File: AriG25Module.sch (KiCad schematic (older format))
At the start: 9 parts

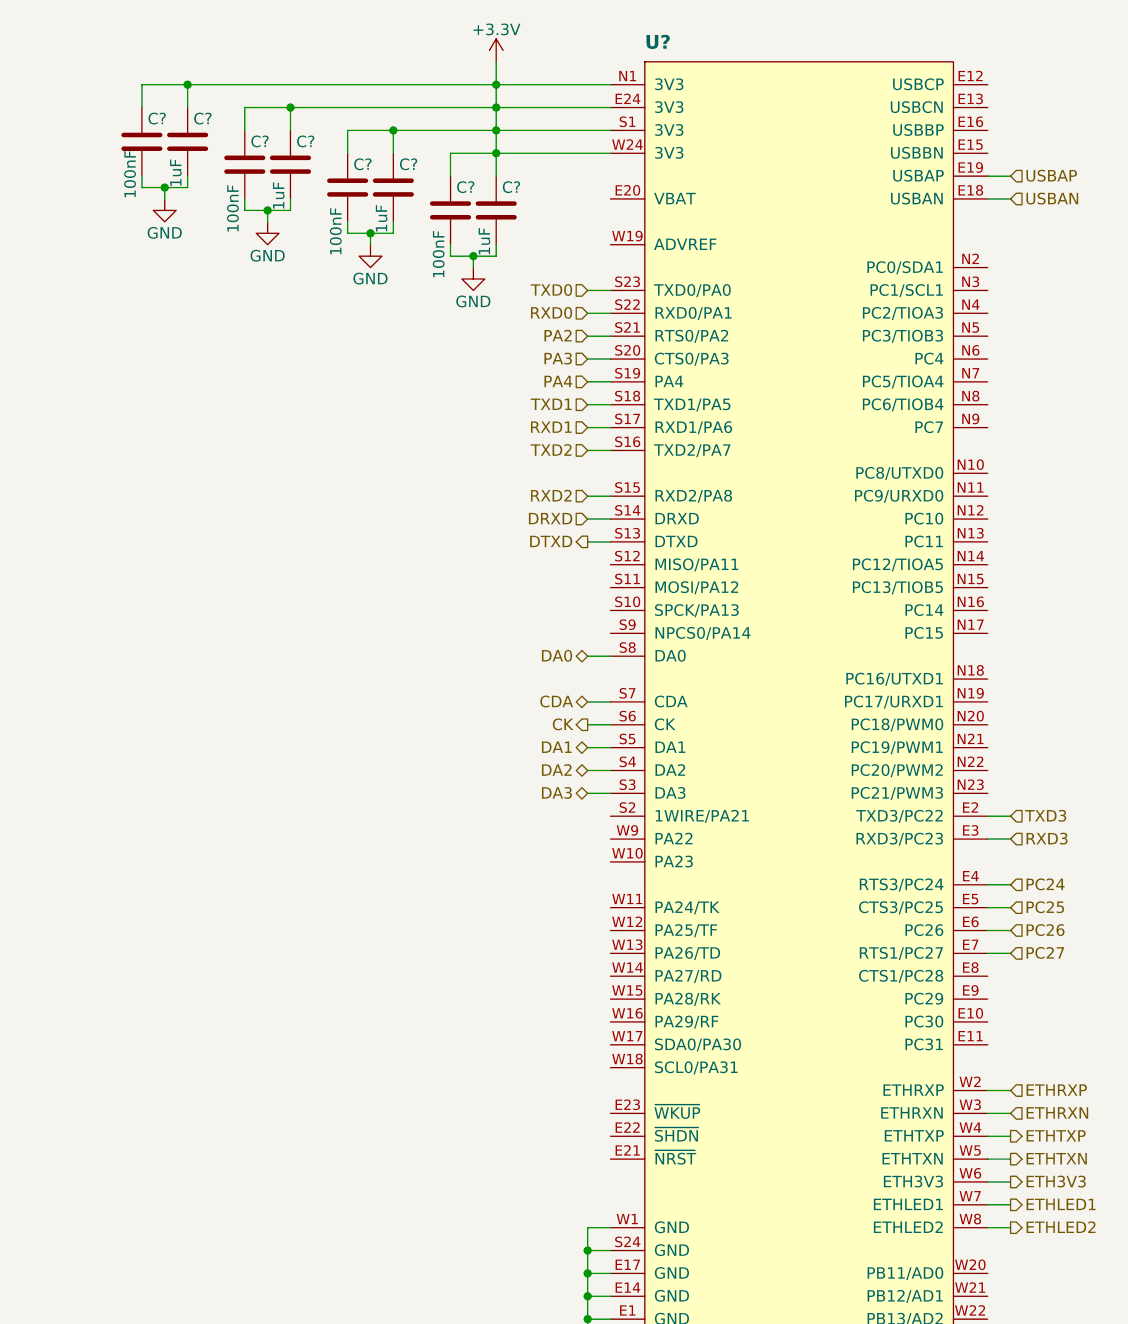
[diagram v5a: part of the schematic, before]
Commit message: Added to scheamtic.
Added reset circuit for Aiya, power led for 3V3 line, USB type A connectors for USBB and USBC.
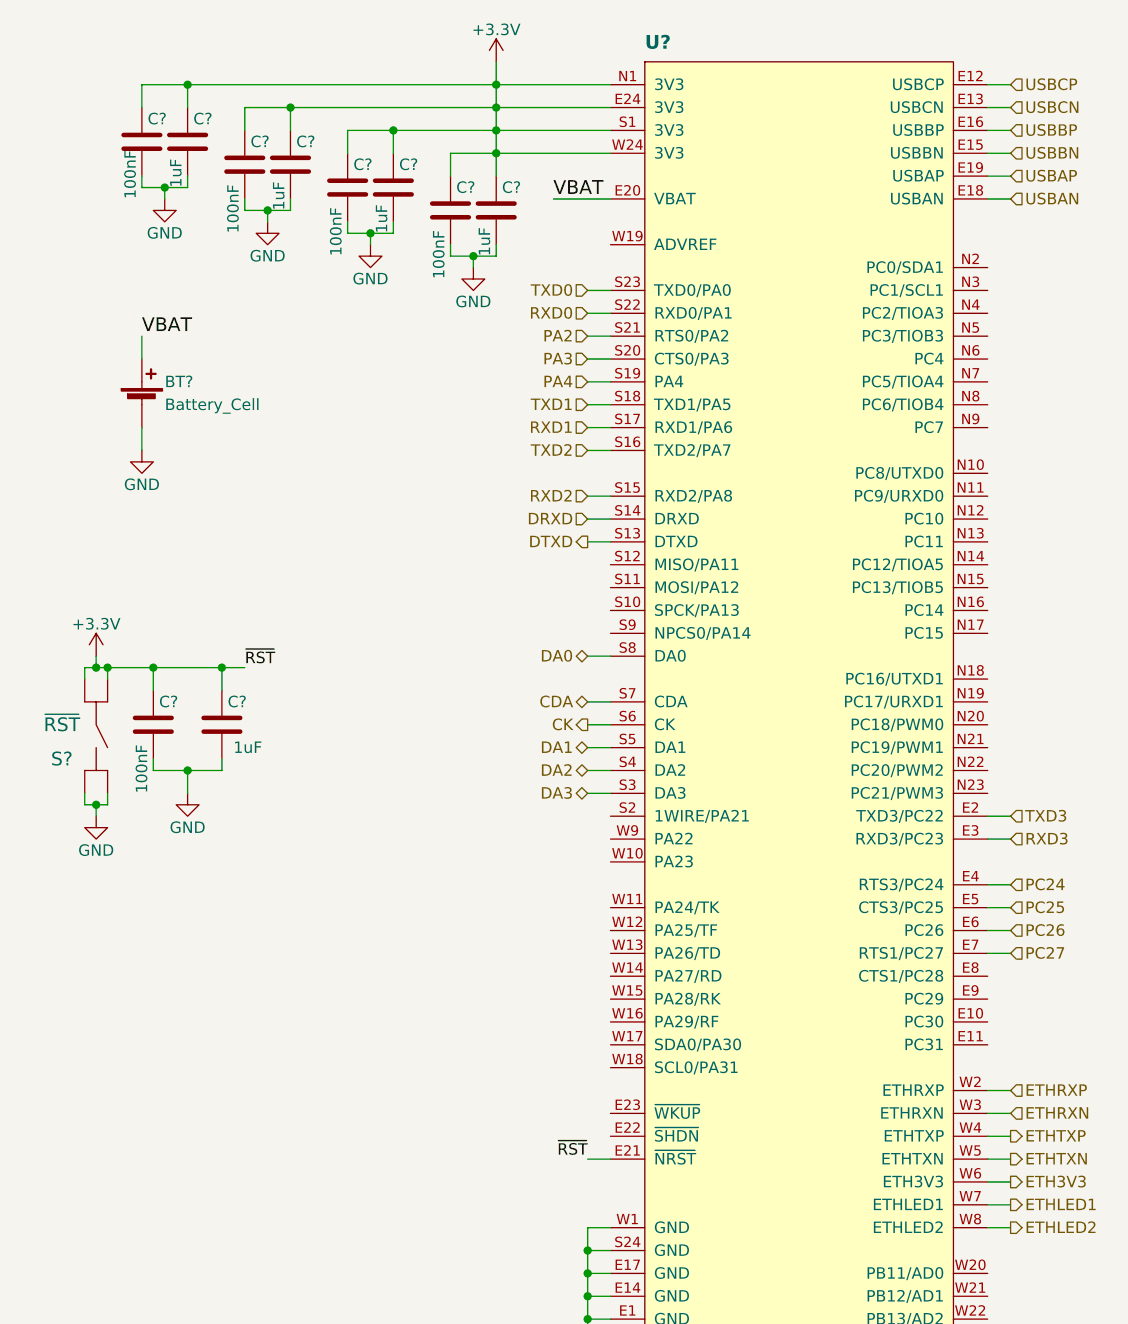
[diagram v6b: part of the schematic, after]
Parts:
- added BT?: Battery_Cell, symbol Battery_Cell
- added C?: 100nF, symbol C
- added C?: 1uF, symbol C
- added S?: ~RST, symbol SW_TACT
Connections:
- net +3V3: now also U?.E21 (~NRST), C?.1, C?.1, S?.1, S?.2
- net GND: now also BT?.2 (-), C?.2, C?.2, S?.3, S?.4, S?.5 (GND)
- net USBCP: now reaches U?.E12 (USBCP)
- net USBCN: now reaches U?.E13 (USBCN)
- net USBBN: now reaches U?.E15 (USBBN)
- net USBBP: now reaches U?.E16 (USBBP)
- net VBAT: now reaches U?.E20 (VBAT)
- net VBAT: now also BT?.1 (+)
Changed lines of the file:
@@
 LIBS:w_connectors
 LIBS:max-lin
+LIBS:IHE
 LIBS:E-GIF-M-Board-cache
 EELAYER 25 0
@@
 Wire Wire Line
 	3900 2700 4000 2700
+$Comp
+L Battery_Cell BT?
+U 1 1 58979BCB
+P 1950 2800
+F 0 "BT?" H 2050 2900 50  0000 L CNN
+F 1 "Battery_Cell" H 2050 2800 50  0000 L CNN
+F 2 "" V 1950 2860 50  0000 C CNN
+F 3 "" V 1950 2860 50  0000 C CNN
+	1    1950 2800
+	1    0    0    -1
+$EndComp
+Text Label 1950 2500 0    60   ~ 0
+VBAT
+$Comp
+L GND #PWR?
+U 1 1 58979EE3
+P 1950 3000
+F 0 "#PWR?" H 1950 2750 50  0001 C CNN
+F 1 "GND" H 1950 2850 50  0000 C CNN
+F 2 "" H 1950 3000 50  0000 C CNN
+F 3 "" H 1950 3000 50  0000 C CNN
+	1    1950 3000
+	1    0    0    -1
+$EndComp
+Wire Wire Line
+	1950 3000 1950 2900
+Wire Wire Line
+	1950 2600 1950 2500
+Text Label 3750 1900 0    60   ~ 0
+VBAT
+Wire Wire Line
+	3750 1900 4000 1900
+Text HLabel 5750 1700 2    50   Input ~ 0
+USBBN
+Text HLabel 5750 1600 2    50   Input ~ 0
+USBBP
+Text HLabel 5750 1400 2    50   Input ~ 0
+USBCP
+Text HLabel 5750 1500 2    50   Input ~ 0
+USBCN
+Wire Wire Line
+	5650 1400 5750 1400
+Wire Wire Line
+	5650 1500 5750 1500
+Wire Wire Line
+	5650 1600 5750 1600
+Wire Wire Line
+	5650 1700 5750 1700
+$Comp
+L SW_TACT S?
+U 1 1 5897AD81
+P 1750 4250
+F 0 "S?" V 1850 4100 60  0000 C CNN
+F 1 "~RST" V 1700 4100 60  0000 C CNN
+F 2 "" H 1750 4250 60  0000 C CNN
+F 3 "" H 1750 4250 60  0000 C CNN
+	1    1750 4250
+	0    1    1    0
+$EndComp
+$Comp
+L +3.3V #PWR?
+U 1 1 5897B046
+P 1750 3900
+F 0 "#PWR?" H 1750 3750 50  0001 C CNN
+F 1 "+3.3V" H 1750 4040 50  0000 C CNN
+F 2 "" H 1750 3900 50  0000 C CNN
+F 3 "" H 1750 3900 50  0000 C CNN
+	1    1750 3900
+	1    0    0    -1
+$EndComp
+$Comp
+L C C?
+U 1 1 5897B164
+P 2000 4200
+F 0 "C?" H 2025 4300 50  0000 L CNN
+F 1 "100nF" V 1950 3900 50  0000 L CNN
+F 2 "" H 2038 4050 50  0000 C CNN
+F 3 "" H 2000 4200 50  0000 C CNN
+	1    2000 4200
+	1    0    0    -1
+$EndComp
+$Comp
+L C C?
+U 1 1 5897B1B2
+P 2300 4200
+F 0 "C?" H 2325 4300 50  0000 L CNN
+F 1 "1uF" H 2350 4100 50  0000 L CNN
+F 2 "" H 2338 4050 50  0000 C CNN
+F 3 "" H 2300 4200 50  0000 C CNN
+	1    2300 4200
+	1    0    0    -1
+$EndComp
+$Comp
+L GND #PWR?
+U 1 1 5897B24B
+P 2150 4500
+F 0 "#PWR?" H 2150 4250 50  0001 C CNN
+F 1 "GND" H 2150 4350 50  0000 C CNN
+F 2 "" H 2150 4500 50  0000 C CNN
+F 3 "" H 2150 4500 50  0000 C CNN
+	1    2150 4500
+	1    0    0    -1
+$EndComp
+$Comp
+L GND #PWR?
+U 1 1 5897B2E1
+P 1750 4600
+F 0 "#PWR?" H 1750 4350 50  0001 C CNN
+F 1 "GND" H 1750 4450 50  0000 C CNN
+F 2 "" H 1750 4600 50  0000 C CNN
+F 3 "" H 1750 4600 50  0000 C CNN
+	1    1750 4600
+	1    0    0    -1
+$EndComp
+Wire Wire Line
+	1700 4500 1700 4550
+Wire Wire Line
+	1700 4550 1800 4550
+Wire Wire Line
+	1800 4550 1800 4500
+Wire Wire Line
+	1750 4550 1750 4600
+Connection ~ 1750 4550
+Wire Wire Line
+	1700 4000 1700 3950
+Wire Wire Line
+	1700 3950 2400 3950
+Wire Wire Line
+	1750 3950 1750 3900
+Wire Wire Line
+	1800 3950 1800 4000
+Connection ~ 1750 3950
+Wire Wire Line
+	2300 3950 2300 4050
+Connection ~ 1800 3950
+Wire Wire Line
+	2000 4050 2000 3950
+Connection ~ 2000 3950
+Wire Wire Line
+	2300 4350 2300 4400
+Wire Wire Line
+	2300 4400 2000 4400
+Wire Wire Line
+	2000 4400 2000 4350
+Wire Wire Line
+	2150 4400 2150 4500
+Connection ~ 2150 4400
+Text Label 2400 3950 0    50   ~ 0
+~RST
+Text Label 3900 6100 2    50   ~ 0
+~RST
+Wire Wire Line
+	3900 6100 4000 6100
+Connection ~ 2300 3950
 $EndSCHEMATC

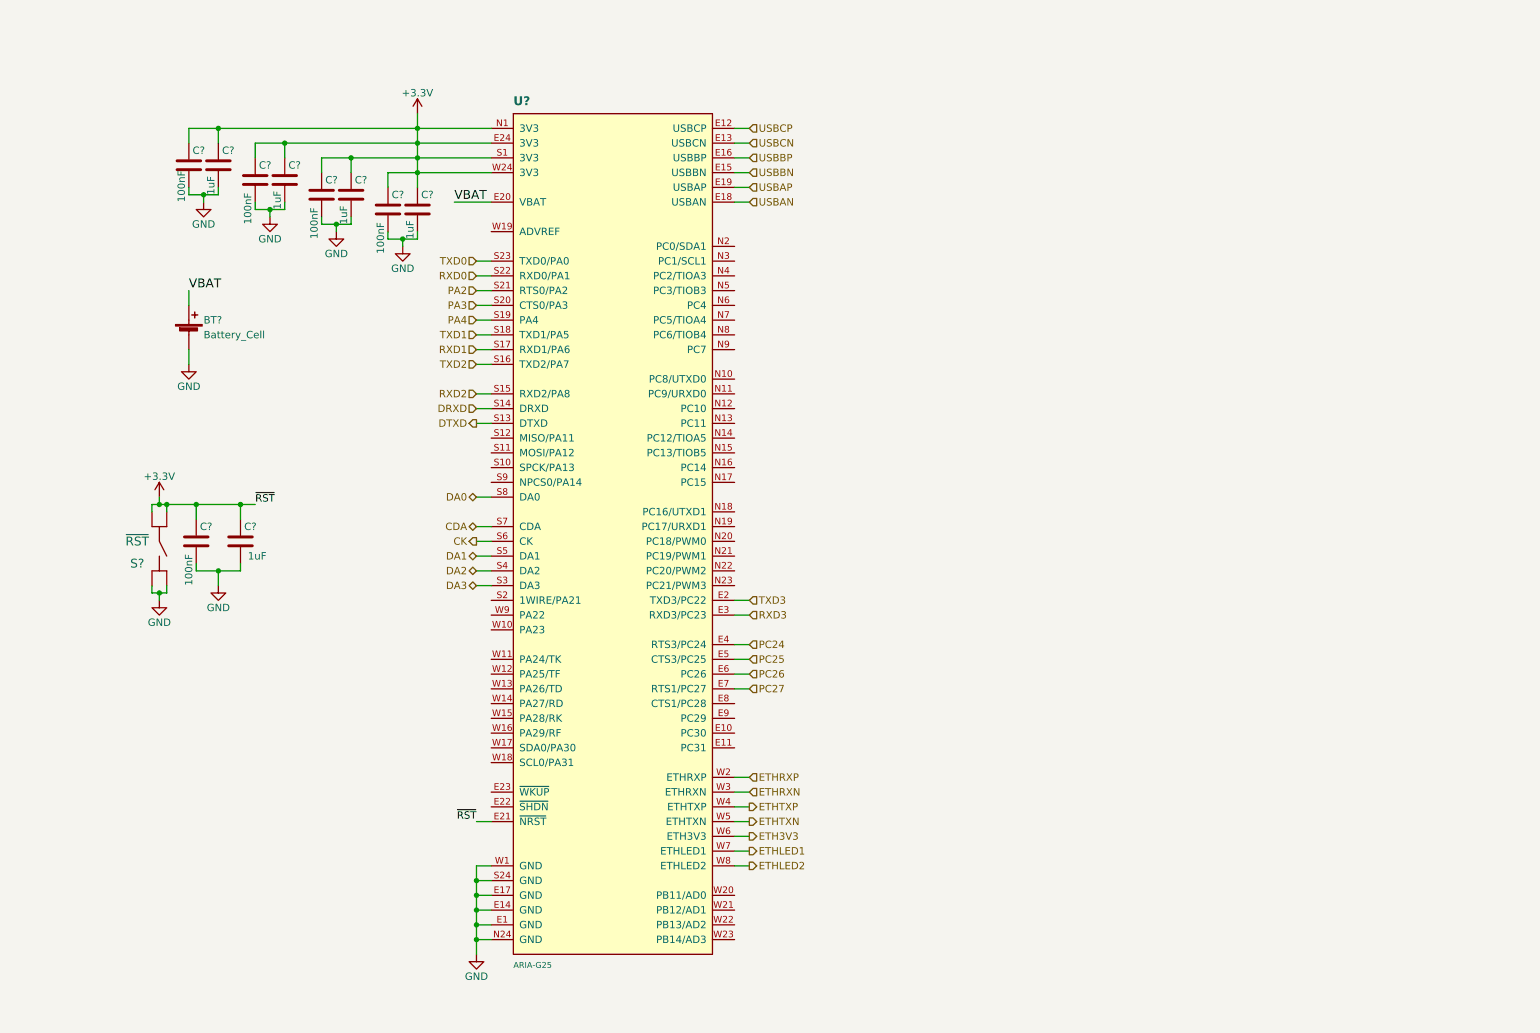
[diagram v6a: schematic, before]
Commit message: Schematic correction
Corrected the direction on some signals. Added a pin header for general development.
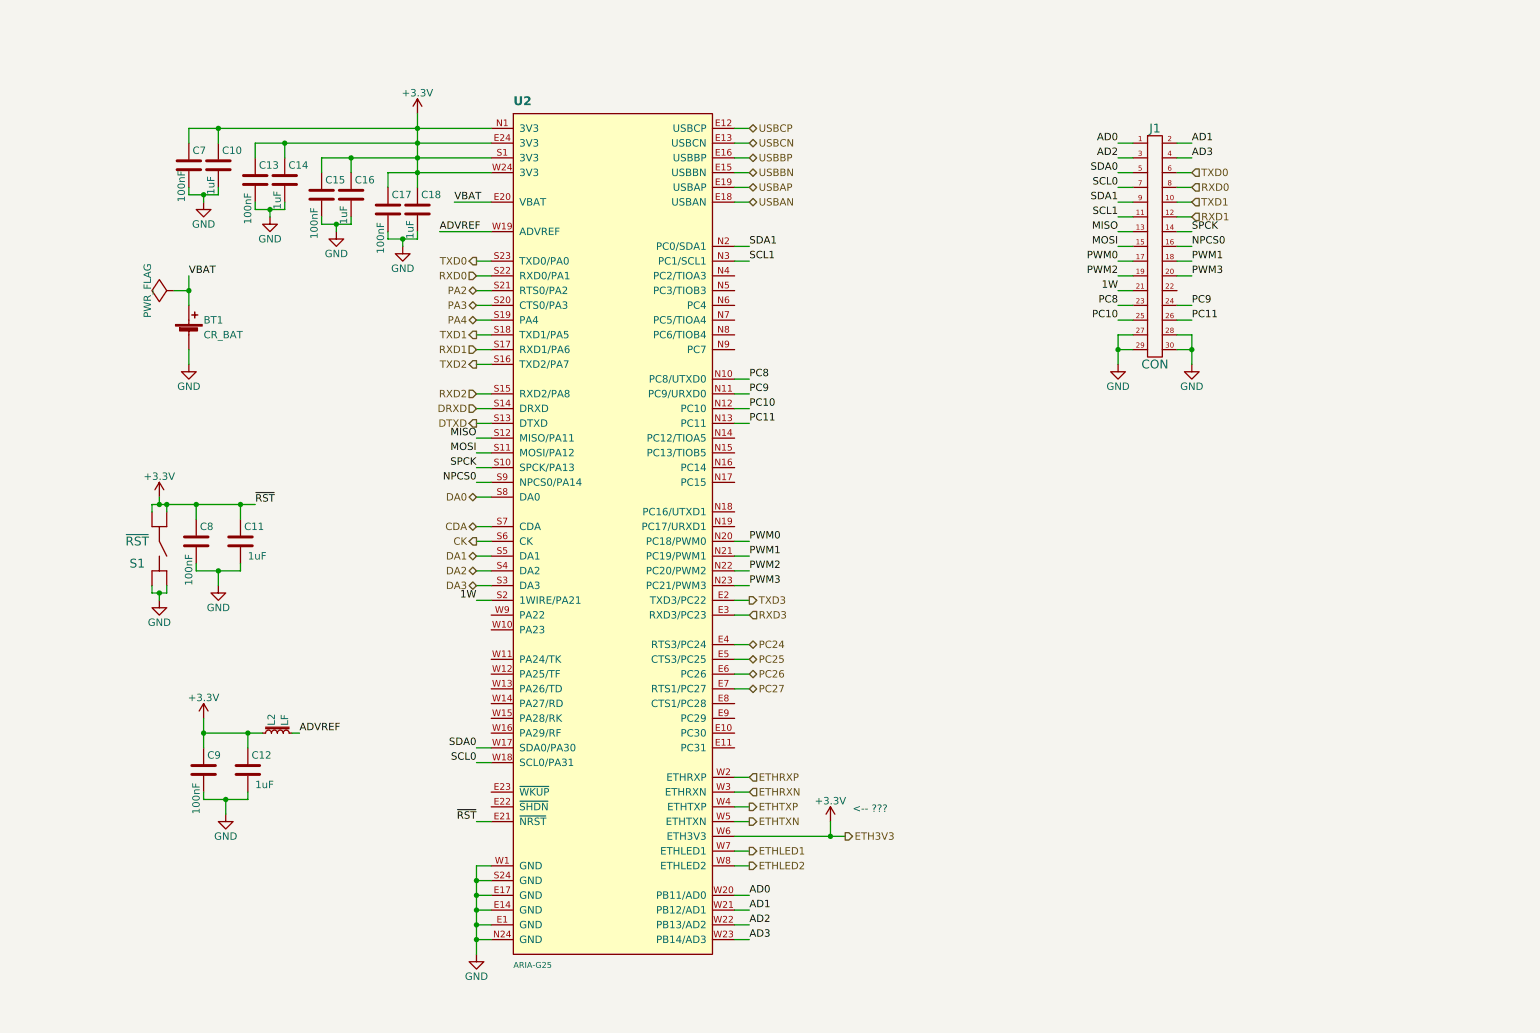
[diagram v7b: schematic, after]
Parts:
- added C12: 1uF, Capacitors_SMD:C_0603_HandSoldering, symbol C
- added C9: 100nF, Capacitors_SMD:C_0603_HandSoldering, symbol C
- added J1: CON, symbol HEADER_15x2
- added L2: LF, symbol L_Core_Iron_Small
- BT1: renamed from BT?; value Battery_Cell -> CR_BAT
- C10, C11, C13, C14, C15, C16, C17, C18, C7, C8: renamed from C?; footprint (none) -> Capacitors_SMD:C_0603_HandSoldering
- U2: renamed from U?; footprint (none) -> misc:ARIA-G25
- gave numbers to parts that had none: 1
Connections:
- net ETH3V3 is gone; now on net +3V3: U2.W6 (ETH3V3)
- net +3V3: now also C12.1, C9.1, L2.1
- net GND: now also C12.2, C9.2, J1.27, J1.28, J1.29, J1.30
- net RXD0: now also J1.8
- net RXD1: now also J1.12
- net TXD0: now also J1.6
- net TXD1: now also J1.10
- net PC8: now reaches U2.N10 (PC8/UTXD0)
- net PC8: now also J1.23
- net PC9: now reaches U2.N11 (PC9/URXD0)
- net PC9: now also J1.24
- net PC10: now reaches U2.N12 (PC10)
- net PC10: now also J1.25
- net PC11: now reaches U2.N13 (PC11)
- net PC11: now also J1.26
- net SDA1: now reaches U2.N2 (PC0/SDA1)
- net SDA1: now also J1.9
- net PWM0: now reaches U2.N20 (PC18/PWM0)
- net PWM0: now also J1.17
- net PWM1: now reaches U2.N21 (PC19/PWM1)
- net PWM1: now also J1.18
- net PWM2: now reaches U2.N22 (PC20/PWM2)
- net PWM2: now also J1.19
- net PWM3: now reaches U2.N23 (PC21/PWM3)
- net PWM3: now also J1.20
- net SCL1: now reaches U2.N3 (PC1/SCL1)
- net SCL1: now also J1.11
- net SPCK: now reaches U2.S10 (SPCK/PA13)
- net SPCK: now also J1.14
- net MOSI: now reaches U2.S11 (MOSI/PA12)
- net MOSI: now also J1.15
- net MISO: now reaches U2.S12 (MISO/PA11)
- net MISO: now also J1.13
- net 1W: now reaches U2.S2 (1WIRE/PA21)
- net 1W: now also J1.21
- net NPCS0: now reaches U2.S9 (NPCS0/PA14)
- net NPCS0: now also J1.16
- net SDA0: now reaches U2.W17 (SDA0/PA30)
- net SDA0: now also J1.5
- net SCL0: now reaches U2.W18 (SCL0/PA31)
- net SCL0: now also J1.7
- net ADVREF: now reaches U2.W19 (ADVREF)
- net ADVREF: now also L2.2
- net AD0: now reaches U2.W20 (PB11/AD0)
- net AD0: now also J1.1
- net AD1: now reaches U2.W21 (PB12/AD1)
- net AD1: now also J1.2
- net AD2: now reaches U2.W22 (PB13/AD2)
- net AD2: now also J1.3
- net AD3: now reaches U2.W23 (PB14/AD3)
- net AD3: now also J1.4
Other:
- note added: "<-- ???"
